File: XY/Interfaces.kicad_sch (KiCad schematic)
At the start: 5 parts, among them J1 200528-0100, J2 200528-0100, U6 USBLC6-2P6

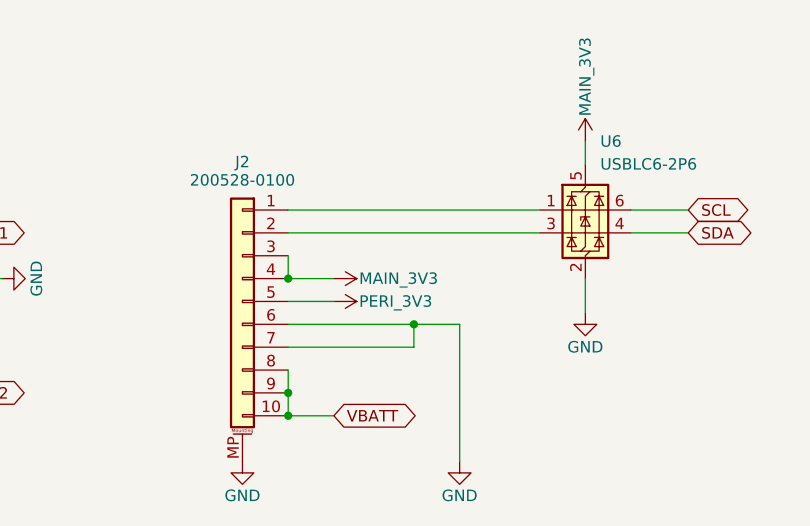
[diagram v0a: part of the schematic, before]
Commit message: Updated layout
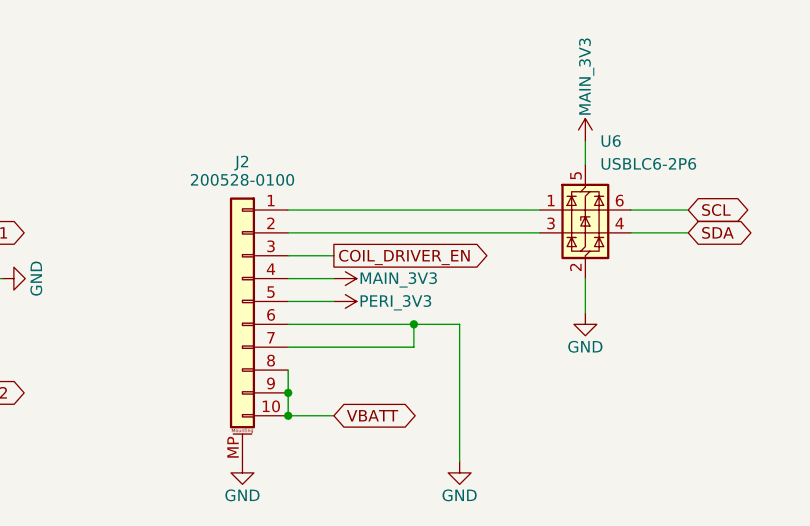
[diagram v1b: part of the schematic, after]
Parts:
- C24, C25: footprint (none) -> Capacitor_SMD:C_0603_1608Metric
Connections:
- net MAIN_3V3: no longer J2.3 (Pin_3)
- new net COIL_DRIVER_EN: J2.3 (Pin_3)
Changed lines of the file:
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@@
 		(color 0 0 0 0)
 	)
-	(junction
-		(at 128.27 88.9)
-		(diameter 0)
-		(color 0 0 0 0)
-	)
 	(wire
 		(pts
@@
 	(wire
 		(pts
-			(xy 128.27 86.36) (xy 128.27 88.9)
-		)
-		(stroke
-			(width 0)
-			(type default)
-		)
-	)
-	(wire
-		(pts
 			(xy 161.29 73.66) (xy 161.29 76.2)
 		)
@@
 		(pts
 			(xy 82.55 88.9) (xy 96.52 88.9)
+		)
+		(stroke
+			(width 0)
+			(type default)
+		)
+	)
+	(wire
+		(pts
+			(xy 128.27 86.36) (xy 133.35 86.36)
 		)
 		(stroke
@@
 		(property "Intersheetrefs" "${INTERSHEET_REFS}"
 			(at 99.8076 101.6 0)
+			(effects
+				(font
+					(size 1.27 1.27)
+				)
+				(justify left)
+				(hide yes)
+			)
+		)
+	)
+	(global_label "COIL_DRIVER_EN"
+		(shape output)
+		(at 133.35 86.36 0)
+		(fields_autoplaced yes)
+		(effects
+			(font
+				(size 1.27 1.27)
+			)
+			(justify left)
+		)
+		(property "Intersheetrefs" "${INTERSHEET_REFS}"
+			(at 151.6357 86.36 0)
 			(effects
 				(font
@@
 			)
 		)
-		(property "Footprint" ""
+		(property "Footprint" "Capacitor_SMD:C_0603_1608Metric"
 			(at 213.36 95.25 0)
 			(effects
@@
 			)
 		)
-		(property "Footprint" ""
+		(property "Footprint" "Capacitor_SMD:C_0603_1608Metric"
 			(at 198.12 95.25 0)
 			(effects

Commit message: Updated 3d models, footprints
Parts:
- J1, J2: footprint Connector_FFC-FPC:Molex_200528-0100_1x10-1MP_P1.00mm_Horizontal -> Argus-Connectors:Molex_200528-0100_1x10-1MP_P1.00mm_Horizontal
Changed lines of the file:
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@@
 			)
 		)
-		(property "Footprint" "Connector_FFC-FPC:Molex_200528-0100_1x10-1MP_P1.00mm_Horizontal"
+		(property "Footprint" "Argus-Connectors:Molex_200528-0100_1x10-1MP_P1.00mm_Horizontal"
 			(at 123.19 91.44 0)
 			(effects
@@
 			)
 		)
-		(property "Footprint" "Connector_FFC-FPC:Molex_200528-0100_1x10-1MP_P1.00mm_Horizontal"
+		(property "Footprint" "Argus-Connectors:Molex_200528-0100_1x10-1MP_P1.00mm_Horizontal"
 			(at 77.47 91.44 0)
 			(effects

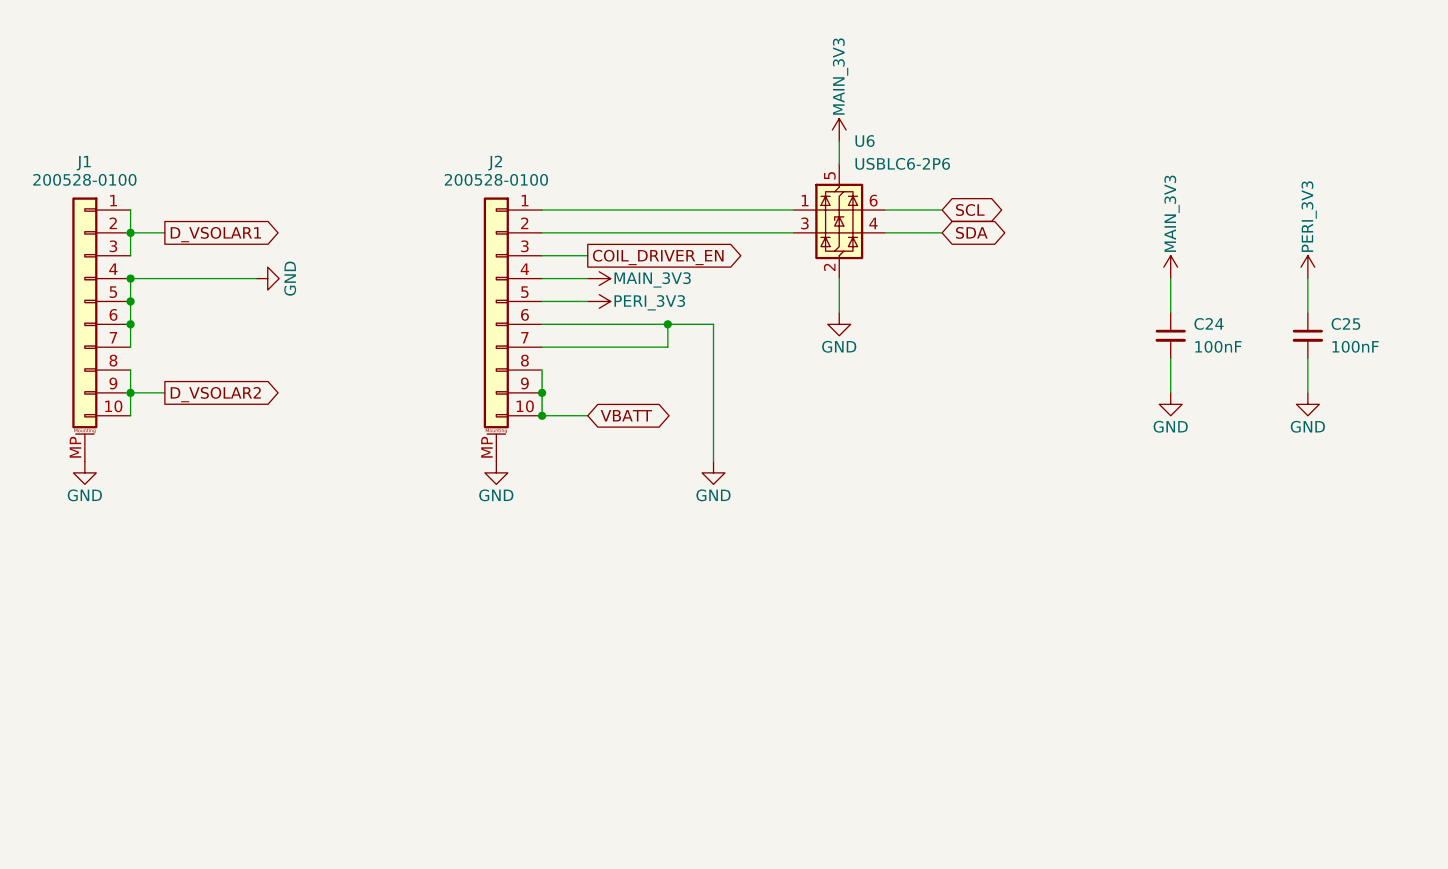
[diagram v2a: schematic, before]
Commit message: Updated silkscreen and jumpers for mainboard compatability
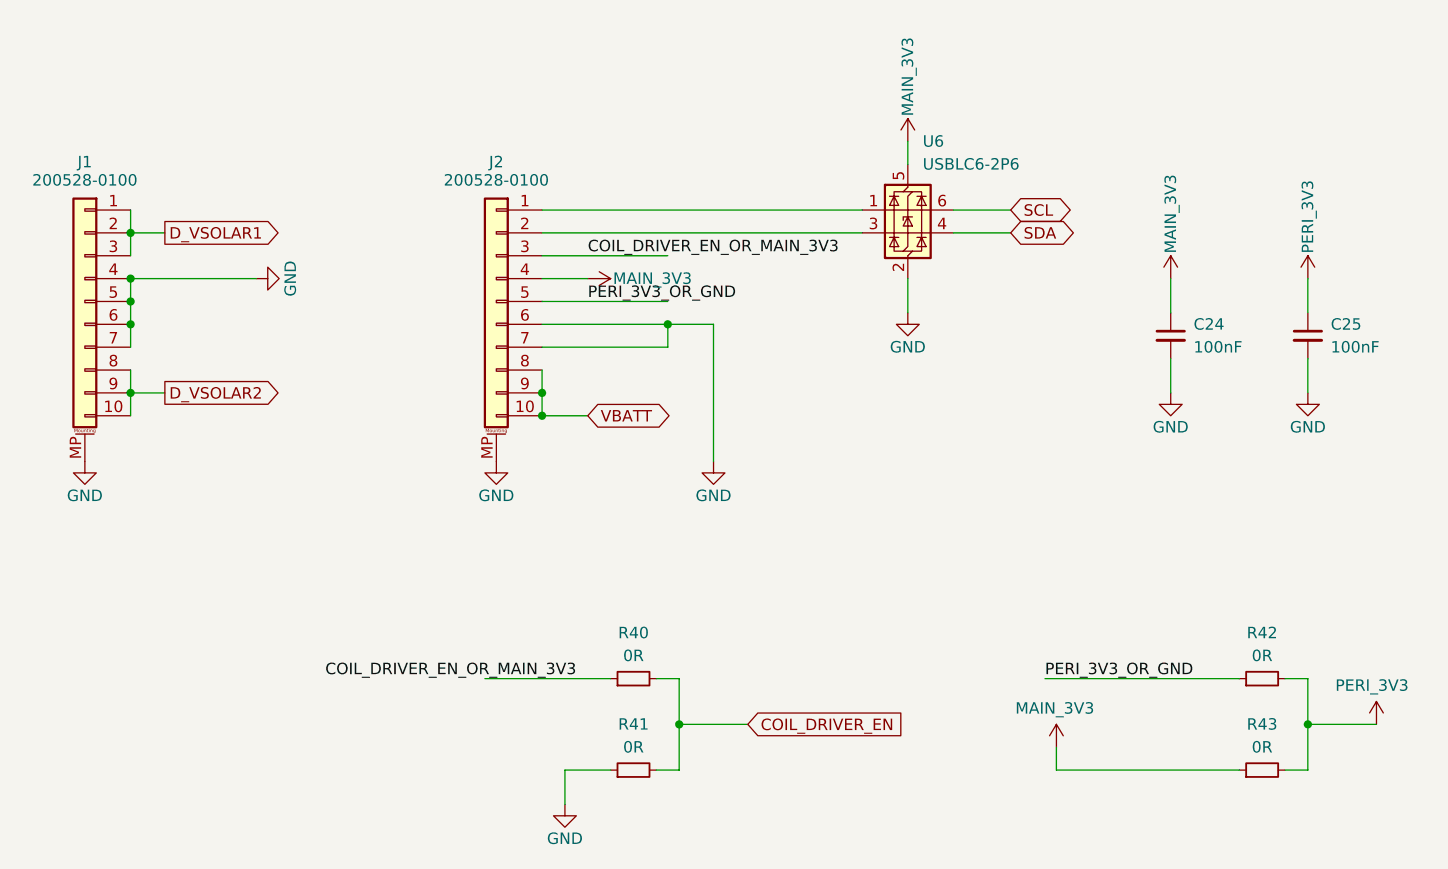
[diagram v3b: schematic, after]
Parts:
- added R40, R41, R42, R43: 0R, Resistor_SMD:R_0603_1608Metric, symbol Device:R_Small
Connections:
- net COIL_DRIVER_EN: now also R40.2, R41.2; no longer J2.3 (Pin_3)
- net GND: now also R41.1
- net MAIN_3V3: now also R43.1
- net PERI_3V3: now also R42.2, R43.2; no longer J2.5 (Pin_5)
- new net COIL_DRIVER_EN_OR_MAIN_3V3: J2.3 (Pin_3), R40.1
- new net PERI_3V3_OR_GND: J2.5 (Pin_5), R42.1
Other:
- moved on the sheet: U6
